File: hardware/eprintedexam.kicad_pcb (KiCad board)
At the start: 2 copper layers, 103 x 98.5 mm, 57 parts, among them J1 Conn_01x04, J2 Conn_01x08, Q1 2N7002, Q2 2N7002, Q3 2N7002, Q4 2N7002, Q5 2N7002, Q6 2N7002, Q7 2N7002, Q8 2N7002, Q9 2N7002, SW1 SW_Push, SW2 SW_Push, SW3 SW_Push, SW4 SW_Push, U1 AP1117-33, U2 ESP-12F

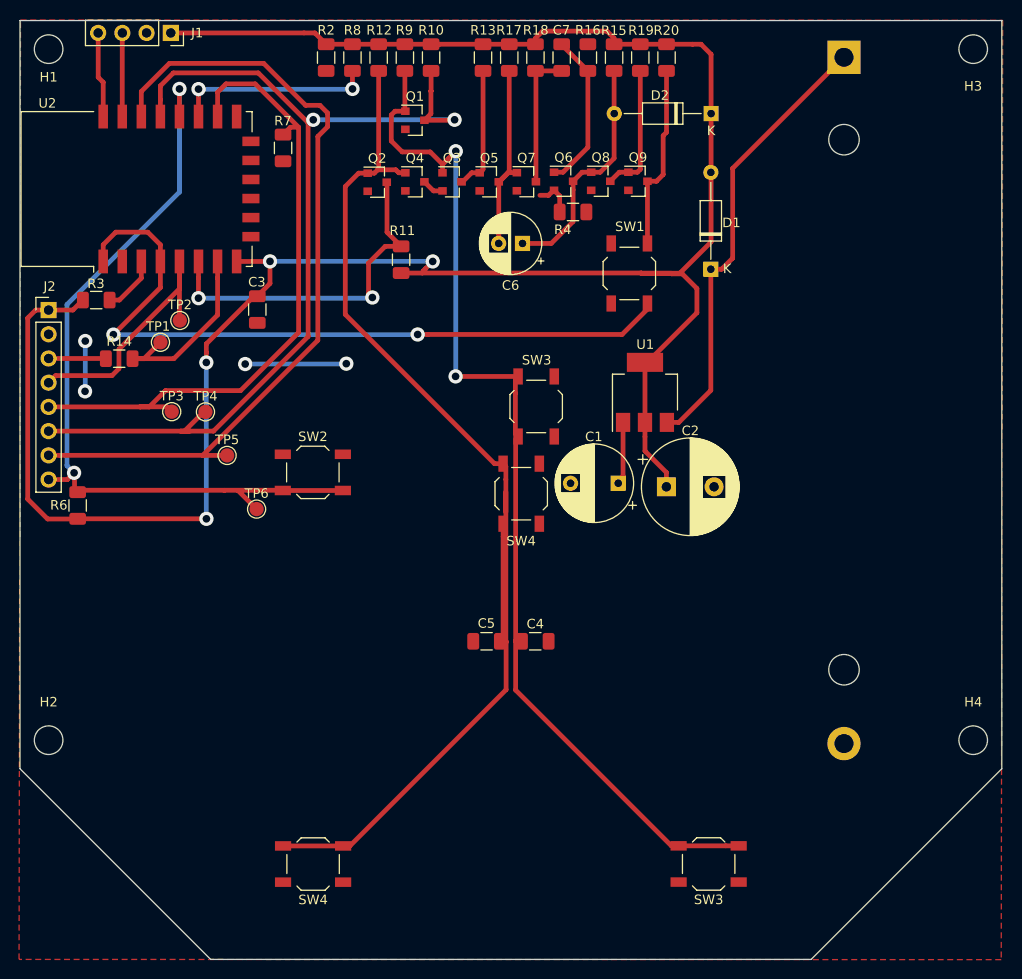
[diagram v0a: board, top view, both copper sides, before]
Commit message: decoupled esp to monostable via button trace
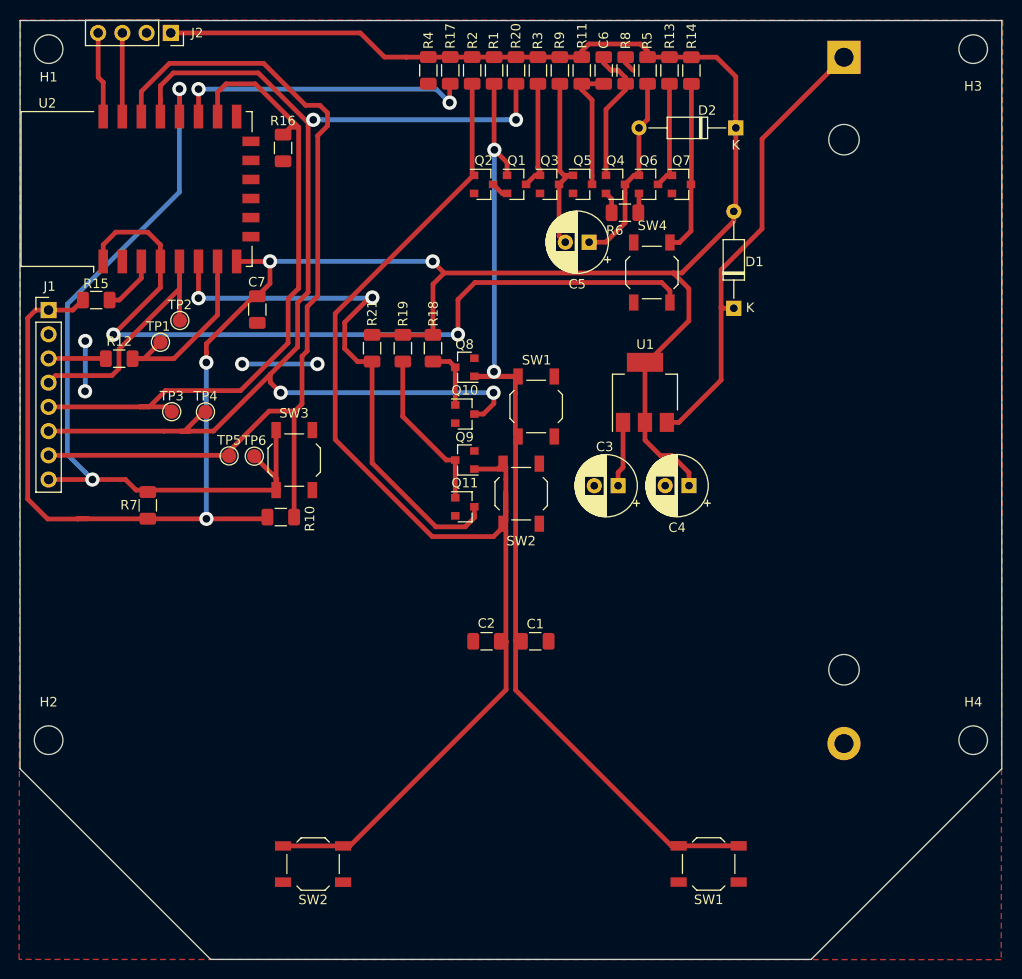
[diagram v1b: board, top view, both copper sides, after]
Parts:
- removed the R12 at (85.6, 16.4)
- removed the R8 at (82.9, 16.4)
- removed the R9 at (88.4, 16.4)
- added Q1: 2N7002, Package_TO_SOT_SMD:SOT-23, F.Cu at (100.1, 29.7)
- added Q11: 2N7002, Package_TO_SOT_SMD:SOT-23, F.Cu at (94.7, 63.5)
- added R1: 5k, Resistor_SMD:R_1206_3216Metric, F.Cu at (97.7, 17.7)
- added R10: 33k, Resistor_SMD:R_1206_3216Metric, F.Cu at (75.4, 64.6)
- added R11: 680k, Resistor_SMD:R_1206_3216Metric, F.Cu at (106.9, 17.7)
- added R17: 10k, Resistor_SMD:R_1206_3216Metric, F.Cu at (93.1, 17.7)
- added R19: 10k, Resistor_SMD:R_1206_3216Metric, F.Cu at (88.2, 46.9)
- added R6: 0, Resistor_SMD:R_1206_3216Metric, F.Cu at (111.5, 32.6)
- C3: renamed from C1; footprint Capacitor_THT:CP_Radial_D8.0mm_P5.00mm -> Capacitor_THT:CP_Radial_D6.3mm_P2.50mm
- C4: renamed from C2; footprint Capacitor_THT:CP_Radial_D10.0mm_P5.00mm -> Capacitor_THT:CP_Radial_D6.3mm_P2.50mm
- R14: renamed from R20; value 1k -> 10k
- R18: value 680k -> 10k
- R2: value 33k -> 5k
- R4: value 0 -> 33k
- moved Q9 34.4 mm to (94.7, 58.6), turned to 180 degrees
- moved R18 32.3 mm to (91.3, 46.9), turned to 90 degrees
- moved Q10 31.3 mm to (94.7, 53.8)
- moved Q8 24.2 mm to (94.7, 48.9), turned to 180 degrees
- moved R4 21.2 mm to (90.8, 17.7), turned to 270 degrees
- moved Q4 21.1 mm to (110.5, 29.7)
- moved Q7 16.3 mm to (117.4, 29.7)
- moved R2 15.4 mm to (95.4, 17.7), turned to 90 degrees
- moved Q2 11.2 mm to (96.6, 29.7)
- moved Q3 10.2 mm to (103.6, 29.7)
- moved Q5 9.79 mm to (107.0, 29.7)
- moved R21 9.77 mm to (84.9, 46.9), turned to 90 degrees
- moved R20 9.01 mm to (100.0, 17.7)
- moved Q6 8.92 mm to (113.9, 29.7)
- moved R7 7.36 mm to (61.4, 63.3)
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- renumbered C4 to C1, C5 to C2, C6 to C5, C7 to C6, C3 to C7, J2 to J1, J1 to J2, Q1 to Q10, R14 to R12, R19 to R13, R3 to R15, R7 to R16, R10 to R20, R11 to R21, R13 to R3, R15 to R5, R6 to R7, R16 to R8, R17 to R9, SW3 to SW1, SW4 to SW2, SW2 to SW3, SW1 to SW4
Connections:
- C5 pad 1: Net-(C6-Pad1) -> Net-(C5-Pad1)
- C6 pad 1: Net-(C7-Pad1) -> Net-(C6-Pad1)
- C6 pad 2: Net-(C7-Pad2) -> Net-(C6-Pad2)
- D2 pad 2: Net-(C6-Pad1) -> Net-(C5-Pad1)
- Q10 pad 1: nxt -> nnxt
- Q2 pad 3: spi-miso_prv-in -> Net-(Q1-Pad2)
- Q3 pad 1: nxt -> Net-(Q1-Pad3)
- Q3 pad 2: Net-(Q3-Pad2) -> GND
- Q3 pad 3: Net-(Q3-Pad3) -> nxt+prv
- Q4 pad 1: prv -> Net-(C6-Pad2)
- Q4 pad 3: Net-(Q3-Pad2) -> Net-(C5-Pad1)
- Q5 pad 1: Net-(Q3-Pad3) -> nxt+prv
- Q5 pad 3: nxt+prv -> Net-(C6-Pad1)
- Q6 pad 1: Net-(C7-Pad2) -> Net-(C5-Pad1)
- Q6 pad 3: Net-(C6-Pad1) -> Net-(Q6-Pad3)
- Q7 pad 1: nxt+prv -> Net-(Q6-Pad3)
- Q7 pad 3: Net-(C7-Pad1) -> nrst
- Q8 pad 1: Net-(C6-Pad1) -> nxt
- Q8 pad 3: Net-(Q8-Pad3) -> nnxt
- Q9 pad 1: Net-(Q8-Pad3) -> prv
- Q9 pad 3: nrst -> nprv
- R13 pad 2: Net-(Q8-Pad3) -> Net-(Q6-Pad3)
- R18 pad 1: VCC -> nnxt
- R18 pad 2: Net-(C7-Pad1) -> VCC
- R2 pad 1: VCC -> prv
- R2 pad 2: GND -> VCC
- R3 pad 1: Net-(Q3-Pad3) -> Net-(Q1-Pad3)
- R4 pad 1: GND -> VCC
- R5 pad 2: Net-(C6-Pad1) -> Net-(C5-Pad1)
- R8 pad 1: Net-(C7-Pad2) -> Net-(C6-Pad2)
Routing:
- net spi-dc_nxt-in: track 103.4 -> 133.3 mm, vias 2 -> 4
- net spi-miso_prv-in: track 37.4 -> 58.0 mm
- net Net-(C5-Pad1): track 0.00 -> 20.5 mm
- net nprv: track 0.00 -> 17.1 mm
- net Net-(C7-Pad2): track 16.6 -> 0.00 mm
- net VCC: track 240.9 -> 256.2 mm
- net Net-(C6-Pad2): track 0.00 -> 14.6 mm
- net Net-(C7-Pad1): track 14.4 -> 0.00 mm
- net Net-(Q8-Pad3): track 14.0 -> 0.00 mm
- net Net-(Q3-Pad3): track 13.0 -> 0.00 mm
- net spi-rst: track 85.6 -> 97.3 mm
- net Net-(C6-Pad1): track 25.0 -> 13.3 mm
- net Net-(Q1-Pad3): track 0.00 -> 11.6 mm
- net Net-(Q6-Pad3): track 0.00 -> 11.6 mm
- net Net-(R17-Pad1): track 21.0 -> 31.8 mm
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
